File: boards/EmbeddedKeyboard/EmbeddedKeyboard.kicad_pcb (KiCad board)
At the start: 2 copper layers, 143.2 x 105.8 mm, 116 parts, among them J1 S2B-PH-SM4-TB, J2 EXTERNAL SWITCH, J8 USB_C_Receptacle_USB2.0_14P, Q1 DMN3135LVT-7, U1 LM3671MFX-3.3_NOPB, U10 MPR121QR2, U11 MPR121QR2, U12 MPR121QR2, U13 MPR121QR2, U14 MPR121QR2, U15 MPR121QR2, U16 MPR121QR2, U17 MPR121QR2, U18 MPR121QR2, U2 MCP73831T-2ACI_OT, U3 ESP32-WROOM-32E, U4 CH340C, U5 TCA9548APWR, U6 MPR121QR2, U7 MPR121QR2, U8 MPR121QR2, U9 MPR121QR2

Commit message: Re-designed keyboard
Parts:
- C1, C10, C11, C12, C13, C14, C15, C16, C2, C22, C24, C25, C26, C27, C28, C29, C3, C30, C31, C32, C33, C34, C4, C5, C50, C51, C6, C7, C8, C9: footprint CL03A104KP3NNNC:CL03A104KP3NNNC -> Capacitor_SMD:C_0402_1005Metric; moved to B.Cu
- C17, C18, C23: footprint CC0805KKX5R5BB106:CC0805KKX5R5BB106 -> Capacitor_Tantalum_SMD:CP_EIA-3216-18_Kemet-A; moved to B.Cu
- C19, C20, C21: footprint CC0805KKX5R5BB106:CC0805KKX5R5BB106 -> Capacitor_SMD:C_0402_1005Metric; moved to B.Cu
- D1, D2, J1, J2, J8, JP1, L1, Q1, S2, S3, U10, U11, U12, U13, U14, U15, U16, U17, U18, U2, U3, U4, U6, U7, U8, U9: moved to B.Cu
- R1, R2: footprint 0402WGF5101TCE:0402WGF5101TCE -> Resistor_SMD:R_0402_1005Metric; moved to B.Cu
- R10: footprint RC0805FR-07100KL:RC0805FR-07100KL -> Resistor_SMD:R_0402_1005Metric; moved to B.Cu
- R11: footprint RC0805FR-072K49L:RC0805FR-072K49L -> Resistor_SMD:R_0402_1005Metric; moved to B.Cu
- R12, R14, R15, R16, R20, R21, R24, R26, R28, R3, R30, R32, R34, R36, R38, R4, R40, R42, R44, R5, R6, R9: footprint AF0805FR-0710KL:AF0805FR-0710KL -> Resistor_SMD:R_0402_1005Metric; moved to B.Cu
- R13, R19: footprint RE0805FRE071KL:RE0805FRE071KL -> Resistor_SMD:R_0402_1005Metric; moved to B.Cu
- R17, R18: footprint RTT01513JTH:RTT01513JTH -> Resistor_SMD:R_0402_1005Metric; moved to B.Cu
- R22, R23, R25, R27, R29, R31, R33, R35, R37, R39, R41, R43, R45: footprint RT0805FRE0775KL:RT0805FRE0775KL -> Resistor_SMD:R_0402_1005Metric; moved to B.Cu
- R7, R8: value 10K -> 22R; footprint AF0805FR-0710KL:AF0805FR-0710KL -> Resistor_SMD:R_0402_1005Metric; moved to B.Cu
- U1: footprint CC0805KKX5R5BB106:CC0805KKX5R5BB106 -> SSW:SOT95P280X145-5N; moved to B.Cu
- U5: footprint MCP73831T-2ACI-OT:MCP73831T-2ACI-OT -> symbols:SOP65P640X120-24N; moved to B.Cu
- moved C10 219.1 mm to (205.1, 52.5)
- moved C5 218.1 mm to (200.5, 54.0)
- moved C9 213.0 mm to (222.1, 95.1), turned to 180 degrees
- moved C6 209.9 mm to (187.6, 52.3)
- moved C24 207.9 mm to (217.6, 96.7), turned to 180 degrees
- moved C2 207.6 mm to (215.7, 99.3), turned to -90 degrees
- moved C14 202.2 mm to (217.4, 103.6), turned to -90 degrees
- moved U10 200.4 mm to (203.9, 55.5), turned to -90 degrees
- moved C29 197.1 mm to (183.0, 53.8)
- moved C51 190.2 mm to (220.5, 146.6)
- moved C22 188.9 mm to (214.6, 153.2), turned to 90 degrees
- moved U3 186.8 mm to (216.8, 133.9), turned to 90 degrees
- moved U13 184.2 mm to (218.8, 93.8), turned to 90 degrees
- moved C4 183.9 mm to (156.9, 52.2)
- moved C12 181.5 mm to (198.2, 128.0), turned to -90 degrees
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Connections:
- U3 pad 10: IRQ2 -> IRQ11
- U3 pad 11: IRQ3 -> IRQ10
- U3 pad 12: IRQ4 -> IRQ1
- U3 pad 13: IRQ5 -> IRQ9
- U3 pad 16: IRQ6 -> IRQ8
- U3 pad 27: IRQ9 -> IRQ5
- U3 pad 28: IRQ10 -> IRQ0
- U3 pad 30: IRQ11 -> IRQ3
- U3 pad 31: IRQ12 -> IRQ2
- U3 pad 7: IRQ8 -> IRQ6
- U3 pad 8: IRQ0 -> IRQ4
- U3 pad 9: IRQ1 -> IRQ12
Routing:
- net IRQ12: track 0.00 -> 195.0 mm, vias 0 -> 2
- net IRQ10: track 0.00 -> 181.8 mm, vias 0 -> 2
- net IRQ9: track 0.00 -> 159.4 mm, vias 0 -> 2
- net SCL6: track 0.00 -> 145.7 mm, vias 0 -> 2
- net SDA6: track 0.00 -> 143.3 mm, vias 0 -> 2
- net SDA5: track 0.00 -> 139.8 mm, vias 0 -> 3
- net SCL5: track 0.00 -> 136.2 mm, vias 0 -> 3
- net IRQ1: track 0.00 -> 132.8 mm, vias 0 -> 2
- net SDA4: track 0.00 -> 124.0 mm, vias 0 -> 3
- net SCL4: track 0.00 -> 122.3 mm, vias 0 -> 3
- net IRQ4: track 0.00 -> 120.0 mm, vias 0 -> 2
- net SDA2: track 0.00 -> 112.0 mm, vias 0 -> 3
- net SCL2: track 0.00 -> 109.0 mm, vias 0 -> 3
- net IRQ2: track 0.00 -> 108.1 mm, vias 0 -> 2
- net SCL1: track 0.00 -> 101.2 mm, vias 0 -> 4
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- added copper zone on In1.Cu, net +3.3V
- added copper zone on In1.Cu, net +5V
- added copper zone on B.Cu, net GND
- added copper zone on F.Cu, net GND
- added copper zone on In2.Cu, net GND
- added copper zone on In1.Cu, net VB+
- added copper zone on In1.Cu, net VBo+
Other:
- copper layers 2 -> 4
- board text added: "0"
- board text added: "1"
- board text added: "10"
- board text added: "11"
- board text added: "2"
- board text added: "3"
- board text added: "4"
- board text added: "5"
- board text added: "6"
- board text added: "7"
- board text added: "8"
- board text added: "9"

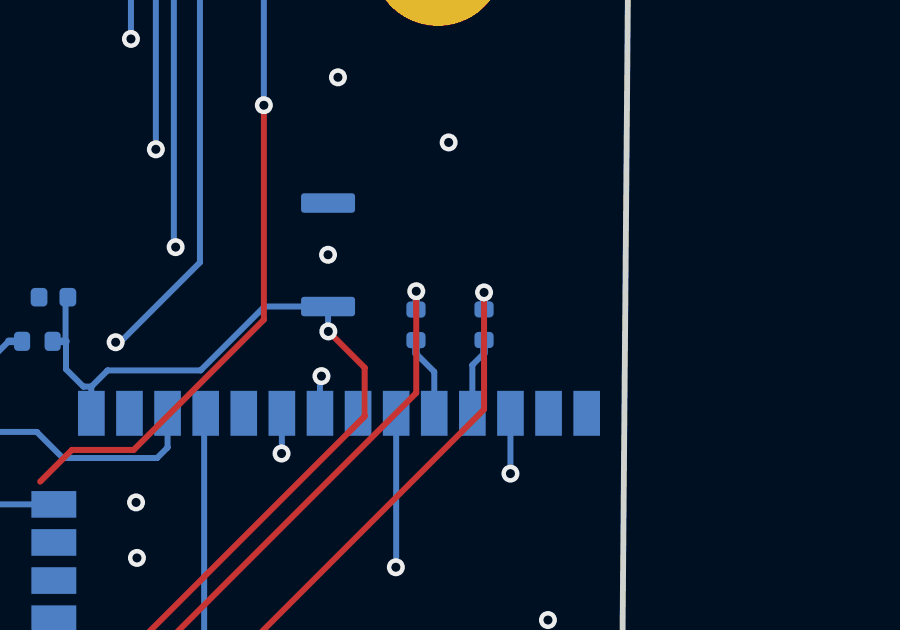
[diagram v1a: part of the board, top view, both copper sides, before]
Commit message: Switch out 22 Ohm resistor 0603 > 0805
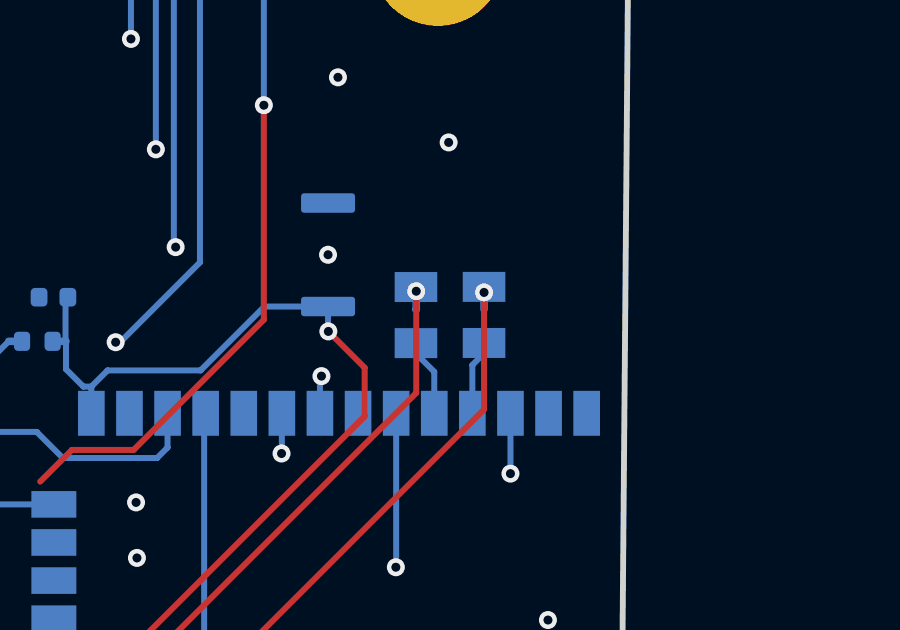
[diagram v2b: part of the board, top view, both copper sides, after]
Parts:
- R7, R8: footprint Resistor_SMD:R_0402_1005Metric -> 0805W8F220JT5E:0805W8F220JT5E
- moved R7 0.33 mm to (216.4, 121.9)
- moved R8 0.33 mm to (218.7, 121.8)
